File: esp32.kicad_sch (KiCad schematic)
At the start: 7 parts, among them J3 USB_C_Receptacle_USB2.0, SW1 SW_Push_Dual_x2, SW3 SW_Push_Dual_x2, U8 ESP32-S3-WROOM-1

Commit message: コンデンサを追加
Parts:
- renumbered SW3 to SW2
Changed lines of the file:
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@@
   (symbol (lib_id "Switch:SW_Push_Dual_x2") (at 86.36 67.31 0) (unit 1)
     (in_bom yes) (on_board yes) (dnp no) (fields_autoplaced)
-    (property "Reference" "SW3" (at 86.36 59.69 0)
+    (property "Reference" "SW2" (at 86.36 59.69 0)
       (effects (font (size 1.27 1.27)))
     )
@@
       (project "mainboard2"
         (path "/106e5476-7cb9-4c2e-b827-12558fe0d8df/a3d63883-59ef-4c72-84e7-54eebcc4b68b"
-          (reference "SW3") (unit 1)
+          (reference "SW2") (unit 1)
         )
       )
@@
       (project "mainboard2"
         (path "/106e5476-7cb9-4c2e-b827-12558fe0d8df/a3d63883-59ef-4c72-84e7-54eebcc4b68b"
-          (reference "R58") (unit 1)
+          (reference "R40") (unit 1)
         )
       )
@@
         )
         (path "/106e5476-7cb9-4c2e-b827-12558fe0d8df/a3d63883-59ef-4c72-84e7-54eebcc4b68b"
-          (reference "R56") (unit 1)
+          (reference "R39") (unit 1)
         )
       )
@@
       (project "mainboard2"
         (path "/106e5476-7cb9-4c2e-b827-12558fe0d8df/a3d63883-59ef-4c72-84e7-54eebcc4b68b"
-          (reference "R57") (unit 1)
-        )
-      )
+          (reference "R41") (unit 1)
+        )
+      )

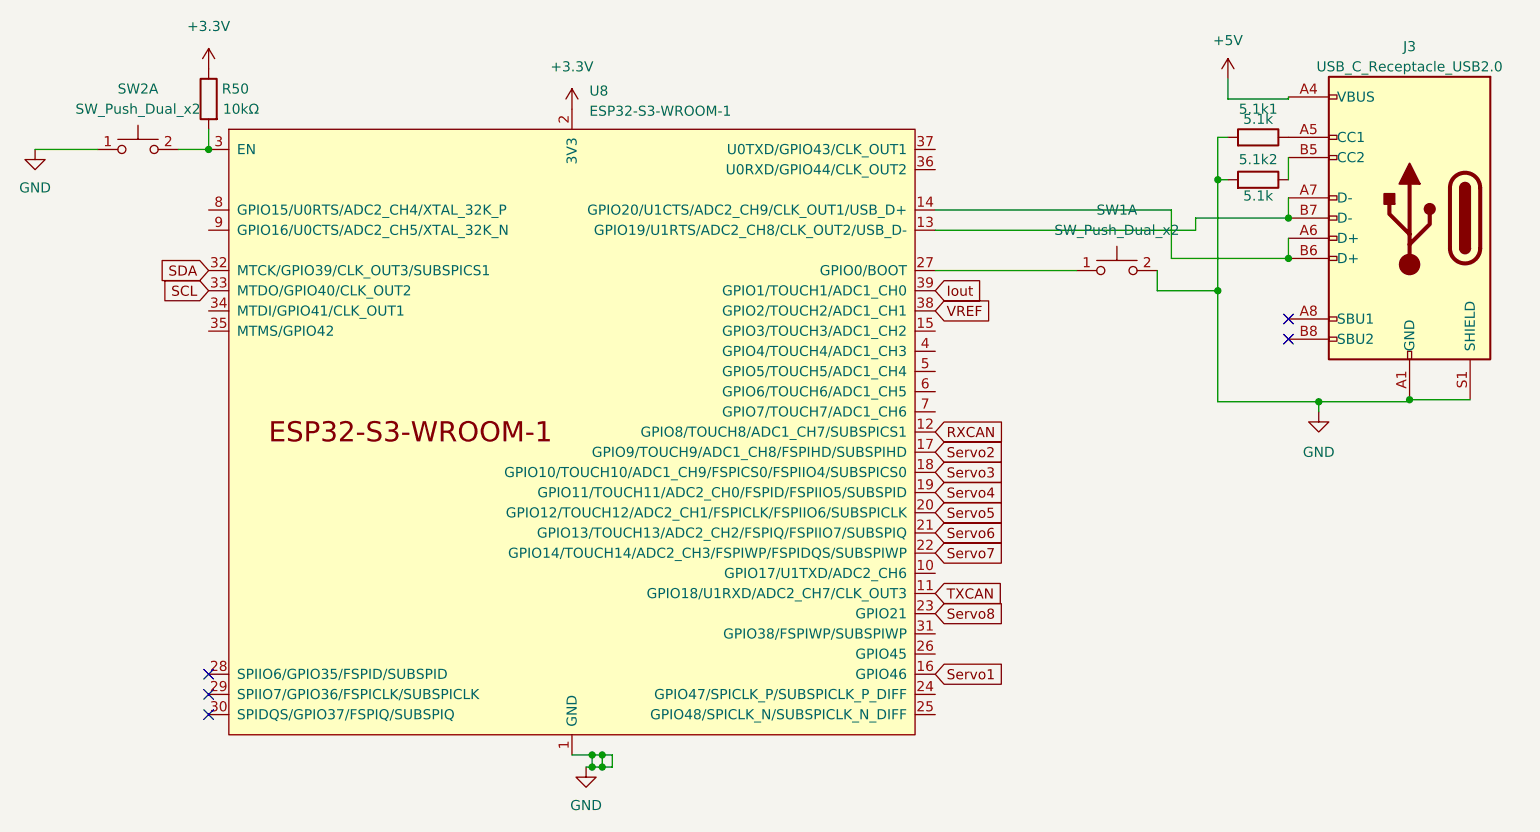
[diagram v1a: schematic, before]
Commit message: 電流センサー変更
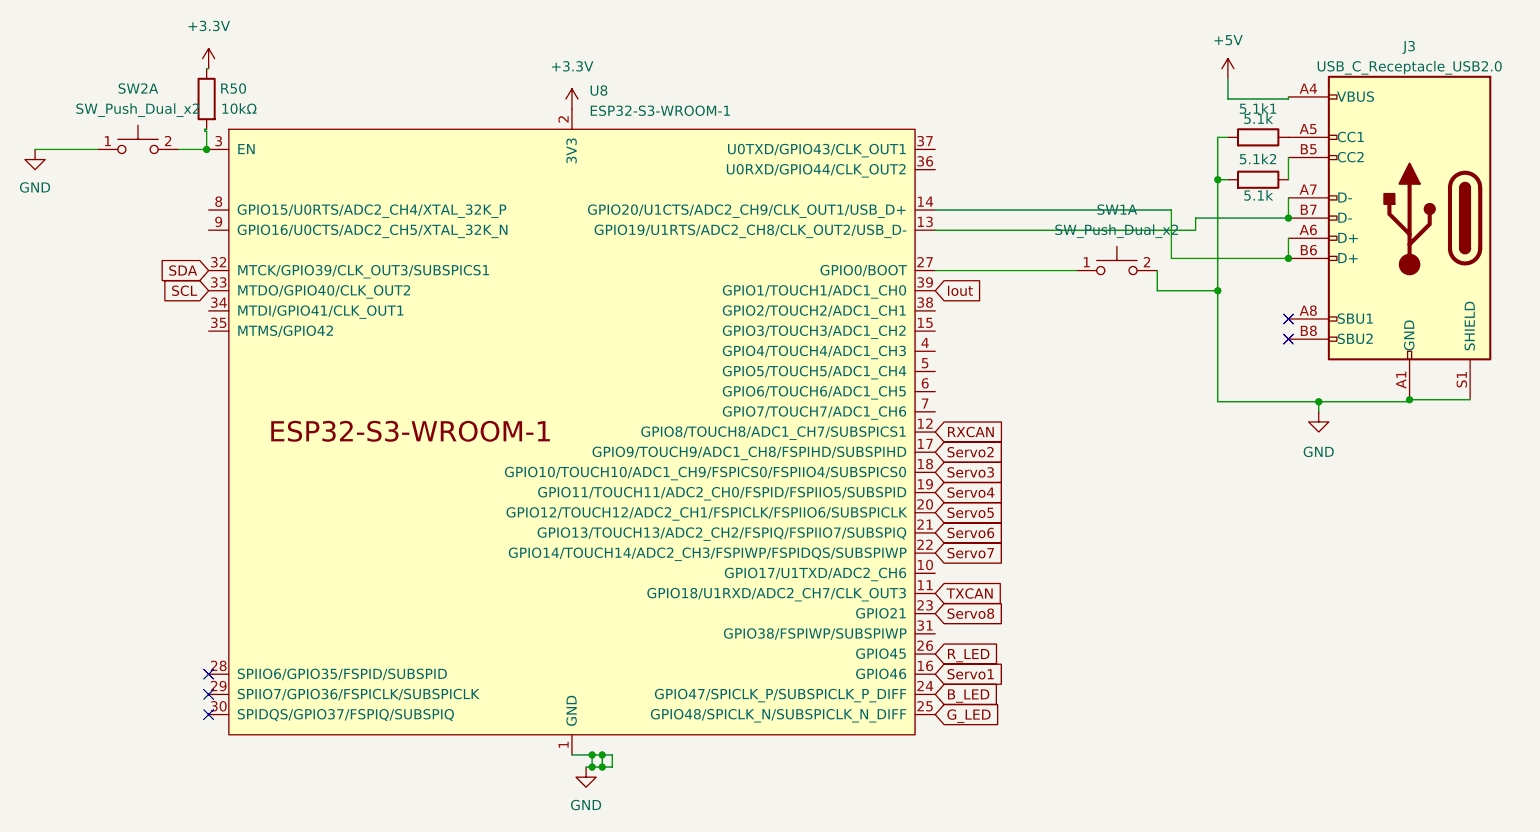
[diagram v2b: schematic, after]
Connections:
- net B_LED: now reaches U8.24 (GPIO47/SPICLK_P/SUBSPICLK_P_DIFF)
- net G_LED: now reaches U8.25 (GPIO48/SPICLK_N/SUBSPICLK_N_DIFF)
- net R_LED: now reaches U8.26 (GPIO45)
- net VREF: no longer names the net of U8.38 (GPIO2/TOUCH2/ADC1_CH1)
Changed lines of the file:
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@@
   (junction (at 143.51 145.034) (diameter 0) (color 0 0 0 0)
   )
-  (junction (at 95.25 67.31) (diameter 0) (color 0 0 0 0)
+  (junction (at 94.996 67.31) (diameter 0) (color 0 0 0 0)
   )
   (junction (at 231.14 81.026) (diameter 0) (color 0 0 0 0)
@@
     (stroke (width 0) (type default))
   )
+  (wire (pts (xy 94.996 57.15) (xy 95.25 57.15))
+    (stroke (width 0) (type default))
+  )
   (wire (pts (xy 222.25 99.06) (xy 234.95 99.06))
     (stroke (width 0) (type default))
@@
     (stroke (width 0) (type default))
   )
-  (wire (pts (xy 95.25 64.77) (xy 95.25 67.31))
+  (wire (pts (xy 94.742 64.77) (xy 94.742 65.024))
     (stroke (width 0) (type default))
   )
@@
     (stroke (width 0) (type default))
   )
+  (wire (pts (xy 94.996 67.31) (xy 95.25 67.31))
+    (stroke (width 0) (type default))
+  )
   (wire (pts (xy 143.51 145.034) (xy 142.748 145.034))
     (stroke (width 0) (type default))
@@
     (stroke (width 0) (type default))
   )
+  (wire (pts (xy 94.742 64.77) (xy 94.996 64.77))
+    (stroke (width 0) (type default))
+  )
   (wire (pts (xy 144.78 145.034) (xy 143.51 145.034))
     (stroke (width 0) (type default))
   )
+  (wire (pts (xy 94.742 65.024) (xy 94.996 65.024))
+    (stroke (width 0) (type default))
+  )
   (wire (pts (xy 216.408 81.026) (xy 231.14 81.026))
     (stroke (width 0) (type default))
@@
     (stroke (width 0) (type default))
   )
+  (wire (pts (xy 94.996 65.024) (xy 94.996 67.31))
+    (stroke (width 0) (type default))
+  )
   (wire (pts (xy 222.25 65.786) (xy 223.52 65.786))
     (stroke (width 0) (type default))
@@
     (stroke (width 0) (type default))
   )
-  (wire (pts (xy 91.44 67.31) (xy 95.25 67.31))
+  (wire (pts (xy 91.44 67.31) (xy 94.996 67.31))
     (stroke (width 0) (type default))
   )
@@
     )
   )
+  (global_label "B_LED" (shape input) (at 186.69 135.89 0) (fields_autoplaced)
+    (effects (font (size 1.27 1.27)) (justify left))
+    (property "Intersheetrefs" "${INTERSHEET_REFS}" (at 195.3599 135.89 0)
+      (effects (font (size 1.27 1.27)) (justify left) hide)
+    )
+  )
   (global_label "Servo5" (shape input) (at 186.69 113.03 0) (fields_autoplaced)
     (effects (font (size 1.27 1.27)) (justify left))
@@
     )
   )
+  (global_label "R_LED" (shape input) (at 186.69 130.81 0) (fields_autoplaced)
+    (effects (font (size 1.27 1.27)) (justify left))
+    (property "Intersheetrefs" "${INTERSHEET_REFS}" (at 195.3599 130.81 0)
+      (effects (font (size 1.27 1.27)) (justify left) hide)
+    )
+  )
   (global_label "RXCAN" (shape input) (at 186.69 102.87 0) (fields_autoplaced)
     (effects (font (size 1.27 1.27)) (justify left))
@@
     )
   )
-  (global_label "VREF" (shape input) (at 186.69 87.63 0) (fields_autoplaced)
-    (effects (font (size 1.27 1.27)) (justify left))
-    (property "Intersheetrefs" "${INTERSHEET_REFS}" (at 194.2714 87.63 0)
+  (global_label "G_LED" (shape input) (at 186.69 138.43 0) (fields_autoplaced)
+    (effects (font (size 1.27 1.27)) (justify left))
+    (property "Intersheetrefs" "${INTERSHEET_REFS}" (at 195.3599 138.43 0)
       (effects (font (size 1.27 1.27)) (justify left) hide)
     )
@@
       (project "mainboard2"
         (path "/106e5476-7cb9-4c2e-b827-12558fe0d8df/a3d63883-59ef-4c72-84e7-54eebcc4b68b"
-          (reference "R40") (unit 1)
+          (reference "R43") (unit 1)
         )
       )
@@
   (symbol (lib_id "power:GND") (at 142.748 145.034 0) (unit 1)
     (in_bom yes) (on_board yes) (dnp no) (fields_autoplaced)
-    (property "Reference" "#PWR0135" (at 142.748 151.384 0)
+    (property "Reference" "#PWR0138" (at 142.748 151.384 0)
       (effects (font (size 1.27 1.27)) hide)
     )
@@
       (project "mainboard2"
         (path "/106e5476-7cb9-4c2e-b827-12558fe0d8df/a3d63883-59ef-4c72-84e7-54eebcc4b68b"
-          (reference "#PWR0135") (unit 1)
+          (reference "#PWR0138") (unit 1)
         )
       )
@@
       (project "mainboard2"
         (path "/106e5476-7cb9-4c2e-b827-12558fe0d8df/a3d63883-59ef-4c72-84e7-54eebcc4b68b"
+          (reference "#PWR0140") (unit 1)
+        )
+      )
+    )
+  )
+  (symbol (lib_id "power:+3.3V") (at 140.97 62.23 0) (unit 1)
+    (in_bom yes) (on_board yes) (dnp no) (fields_autoplaced)
+    (property "Reference" "#PWR0137" (at 140.97 66.04 0)
+      (effects (font (size 1.27 1.27)) hide)
+    )
+    (property "Value" "+3.3V" (at 140.97 56.896 0)
+      (effects (font (size 1.27 1.27)))
+    )
+    (property "Footprint" "" (at 140.97 62.23 0)
+      (effects (font (size 1.27 1.27)) hide)
+    )
+    (property "Datasheet" "" (at 140.97 62.23 0)
+      (effects (font (size 1.27 1.27)) hide)
+    )
+    (pin "1")
+    (instances
+      (project "mainboard2"
+        (path "/106e5476-7cb9-4c2e-b827-12558fe0d8df/a3d63883-59ef-4c72-84e7-54eebcc4b68b"
           (reference "#PWR0137") (unit 1)
         )
@@
     )
   )
-  (symbol (lib_id "power:+3.3V") (at 140.97 62.23 0) (unit 1)
-    (in_bom yes) (on_board yes) (dnp no) (fields_autoplaced)
-    (property "Reference" "#PWR0134" (at 140.97 66.04 0)
-      (effects (font (size 1.27 1.27)) hide)
-    )
-    (property "Value" "+3.3V" (at 140.97 56.896 0)
-      (effects (font (size 1.27 1.27)))
-    )
-    (property "Footprint" "" (at 140.97 62.23 0)
-      (effects (font (size 1.27 1.27)) hide)
-    )
-    (property "Datasheet" "" (at 140.97 62.23 0)
-      (effects (font (size 1.27 1.27)) hide)
-    )
-    (pin "1")
-    (instances
-      (project "mainboard2"
-        (path "/106e5476-7cb9-4c2e-b827-12558fe0d8df/a3d63883-59ef-4c72-84e7-54eebcc4b68b"
-          (reference "#PWR0134") (unit 1)
-        )
-      )
-    )
-  )
-  (symbol (lib_id "Device:R") (at 95.25 60.96 0) (mirror y) (unit 1)
+  (symbol (lib_id "Device:R") (at 94.996 60.96 0) (mirror y) (unit 1)
     (in_bom yes) (on_board yes) (dnp no)
-    (property "Reference" "R50" (at 100.33 59.69 0)
+    (property "Reference" "R50" (at 100.076 59.69 0)
       (effects (font (size 1.27 1.27)) (justify left))
     )
-    (property "Value" "10kΩ" (at 101.6 62.23 0)
+    (property "Value" "10kΩ" (at 101.346 62.23 0)
       (effects (font (size 1.27 1.27)) (justify left))
     )
-    (property "Footprint" "Resistor_SMD:R_0603_1608Metric_Pad0.98x0.95mm_HandSolder" (at 97.028 60.96 90)
-      (effects (font (size 1.27 1.27)) hide)
-    )
-    (property "Datasheet" "~" (at 95.25 60.96 0)
+    (property "Footprint" "Resistor_SMD:R_0603_1608Metric_Pad0.98x0.95mm_HandSolder" (at 96.774 60.96 90)
+      (effects (font (size 1.27 1.27)) hide)
+    )
+    (property "Datasheet" "~" (at 94.996 60.96 0)
       (effects (font (size 1.27 1.27)) hide)
     )
@@
         )
         (path "/106e5476-7cb9-4c2e-b827-12558fe0d8df/a3d63883-59ef-4c72-84e7-54eebcc4b68b"
-          (reference "R39") (unit 1)
+          (reference "R42") (unit 1)
         )
       )
@@
   (symbol (lib_id "power:+5V") (at 223.52 58.42 0) (unit 1)
     (in_bom yes) (on_board yes) (dnp no) (fields_autoplaced)
-    (property "Reference" "#PWR0136" (at 223.52 62.23 0)
+    (property "Reference" "#PWR0139" (at 223.52 62.23 0)
       (effects (font (size 1.27 1.27)) hide)
     )
@@
       (project "mainboard2"
         (path "/106e5476-7cb9-4c2e-b827-12558fe0d8df/a3d63883-59ef-4c72-84e7-54eebcc4b68b"
+          (reference "#PWR0139") (unit 1)
+        )
+      )
+    )
+  )
+  (symbol (lib_id "power:+3.3V") (at 95.25 57.15 0) (unit 1)
+    (in_bom yes) (on_board yes) (dnp no) (fields_autoplaced)
+    (property "Reference" "#PWR0136" (at 95.25 60.96 0)
+      (effects (font (size 1.27 1.27)) hide)
+    )
+    (property "Value" "+3.3V" (at 95.25 51.816 0)
+      (effects (font (size 1.27 1.27)))
+    )
+    (property "Footprint" "" (at 95.25 57.15 0)
+      (effects (font (size 1.27 1.27)) hide)
+    )
+    (property "Datasheet" "" (at 95.25 57.15 0)
+      (effects (font (size 1.27 1.27)) hide)
+    )
+    (pin "1")
+    (instances
+      (project "mainboard2"
+        (path "/106e5476-7cb9-4c2e-b827-12558fe0d8df/a3d63883-59ef-4c72-84e7-54eebcc4b68b"
           (reference "#PWR0136") (unit 1)
-        )
-      )
-    )
-  )
-  (symbol (lib_id "power:+3.3V") (at 95.25 57.15 0) (unit 1)
-    (in_bom yes) (on_board yes) (dnp no) (fields_autoplaced)
-    (property "Reference" "#PWR0133" (at 95.25 60.96 0)
-      (effects (font (size 1.27 1.27)) hide)
-    )
-    (property "Value" "+3.3V" (at 95.25 51.816 0)
-      (effects (font (size 1.27 1.27)))
-    )
-    (property "Footprint" "" (at 95.25 57.15 0)
-      (effects (font (size 1.27 1.27)) hide)
-    )
-    (property "Datasheet" "" (at 95.25 57.15 0)
-      (effects (font (size 1.27 1.27)) hide)
-    )
-    (pin "1")
-    (instances
-      (project "mainboard2"
-        (path "/106e5476-7cb9-4c2e-b827-12558fe0d8df/a3d63883-59ef-4c72-84e7-54eebcc4b68b"
-          (reference "#PWR0133") (unit 1)
         )
       )
@@
   (symbol (lib_id "power:GND") (at 73.406 67.31 0) (unit 1)
     (in_bom yes) (on_board yes) (dnp no) (fields_autoplaced)
-    (property "Reference" "#PWR0132" (at 73.406 73.66 0)
+    (property "Reference" "#PWR0135" (at 73.406 73.66 0)
       (effects (font (size 1.27 1.27)) hide)
     )
@@
       (project "mainboard2"
         (path "/106e5476-7cb9-4c2e-b827-12558fe0d8df/a3d63883-59ef-4c72-84e7-54eebcc4b68b"
-          (reference "#PWR0132") (unit 1)
+          (reference "#PWR0135") (unit 1)
         )
       )
@@
       (project "mainboard2"
         (path "/106e5476-7cb9-4c2e-b827-12558fe0d8df/a3d63883-59ef-4c72-84e7-54eebcc4b68b"
-          (reference "R41") (unit 1)
-        )
-      )
+          (reference "R44") (unit 1)
+        )
+      )

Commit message: ESP32バージョン
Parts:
- removed 5.1k1, 5.1k2: 5.1k, Capacitor_SMD:C_0603_1608Metric_Pad1.08x0.95mm_HandSolder, symbol Device:R
- removed J3: USB_C_Receptacle_USB2.0, Connector_USB:USB_C_Receptacle_HRO_TYPE-C-31-M-12, symbol Connector:USB_C_Receptacle_USB2.0
- removed R50: 10kΩ, Resistor_SMD:R_0603_1608Metric_Pad0.98x0.95mm_HandSolder, symbol Device:R
- removed SW1, SW2: SW_Push_Dual_x2, Button_Switch_SMD:SW_Push_1P1T_NO_CK_KMR2, symbol Switch:SW_Push_Dual_x2
- removed U8: ESP32-S3-WROOM-1, PCM_Espressif:ESP32-S3-WROOM-1, symbol PCM_Espressif:ESP32-S3-WROOM-1
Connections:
- no-connect marks 5 -> 0
